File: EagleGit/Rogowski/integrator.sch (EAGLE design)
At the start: 25 parts, among them IC1 TL061P, IC2 TL061P

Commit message: DPS pro akvarko
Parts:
- added C3, C4, C5, C6: (no value), rcl:C-EU050-035X075
- added C7, C8: (no value), rcl:CPOL-EUE2.5-7
- added PAD10, PAD9: (no value), wirepad:3,81/1,4
- R1, R2, R6: device rcl:R-TRIMMT18 -> pot:TRIM_EU-LI10
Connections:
- removed net N$9: C1.1, IC2.OUT, PAD4.P, R10.1, R12.2
- new net N$11: PAD9.P, R10.1
- new net OUT: C1.1, IC2.OUT, PAD10.P, PAD4.P, R12.2
- net GND: now also C3.2, C5.2, C7.-
- net GND2: now also C3.1, C4.2, C5.1, C6.2, C7.+, C8.-
- net N$3: now also R2.E; no longer R2.A
- net N$4: now also R2.A; no longer R2.E
- net VDD: now also C4.1, C6.1, C8.+

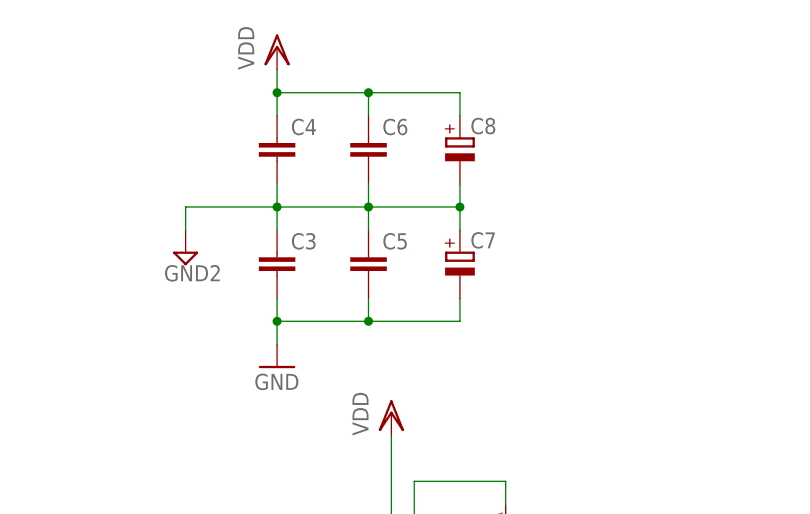
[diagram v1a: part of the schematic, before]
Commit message: Vytvorena cela pro Rogowskiho civku a dodelan budic LED
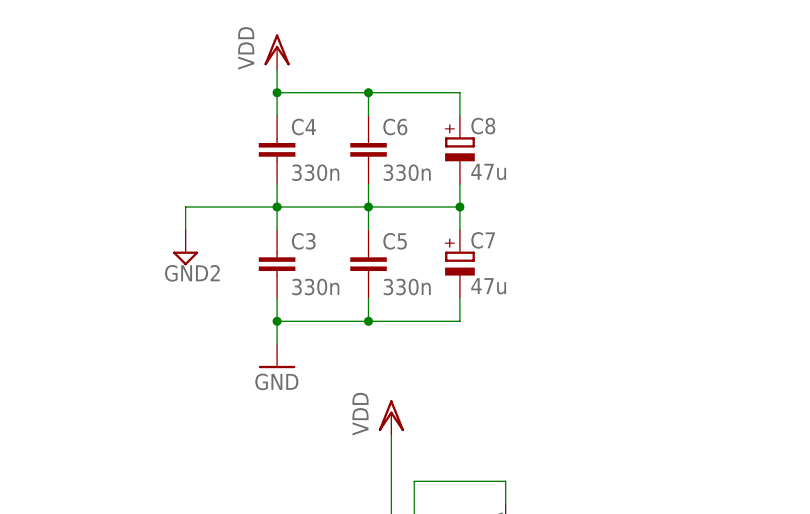
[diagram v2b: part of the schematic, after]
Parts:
- C3, C4, C5, C6: value (none) -> 330n
- C7, C8: value (none) -> 47u
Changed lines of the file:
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@@
 <part name="PAD10" library="wirepad" deviceset="3,81/1,4" device=""/>
 <part name="SUPPLY4" library="supply2" deviceset="GND2" device=""/>
-<part name="C3" library="rcl" deviceset="C-EU" device="050-035X075"/>
-<part name="C4" library="rcl" deviceset="C-EU" device="050-035X075"/>
-<part name="C5" library="rcl" deviceset="C-EU" device="050-035X075"/>
-<part name="C6" library="rcl" deviceset="C-EU" device="050-035X075"/>
+<part name="C3" library="rcl" deviceset="C-EU" device="050-035X075" value="330n"/>
+<part name="C4" library="rcl" deviceset="C-EU" device="050-035X075" value="330n"/>
+<part name="C5" library="rcl" deviceset="C-EU" device="050-035X075" value="330n"/>
+<part name="C6" library="rcl" deviceset="C-EU" device="050-035X075" value="330n"/>
 <part name="VDD5" library="supply1" deviceset="VDD" device=""/>
 <part name="GND9" library="supply1" deviceset="GND" device=""/>
-<part name="C7" library="rcl" deviceset="CPOL-EU" device="E2.5-7"/>
-<part name="C8" library="rcl" deviceset="CPOL-EU" device="E2.5-7"/>
+<part name="C7" library="rcl" deviceset="CPOL-EU" device="E2.5-7" value="47u"/>
+<part name="C8" library="rcl" deviceset="CPOL-EU" device="E2.5-7" value="47u"/>
 </parts>
 <sheets>
